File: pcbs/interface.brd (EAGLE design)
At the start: 36.3 x 29.1 mm, 26 parts, among them U1 ISL3179EIBZ, U2 ATMEGA328P

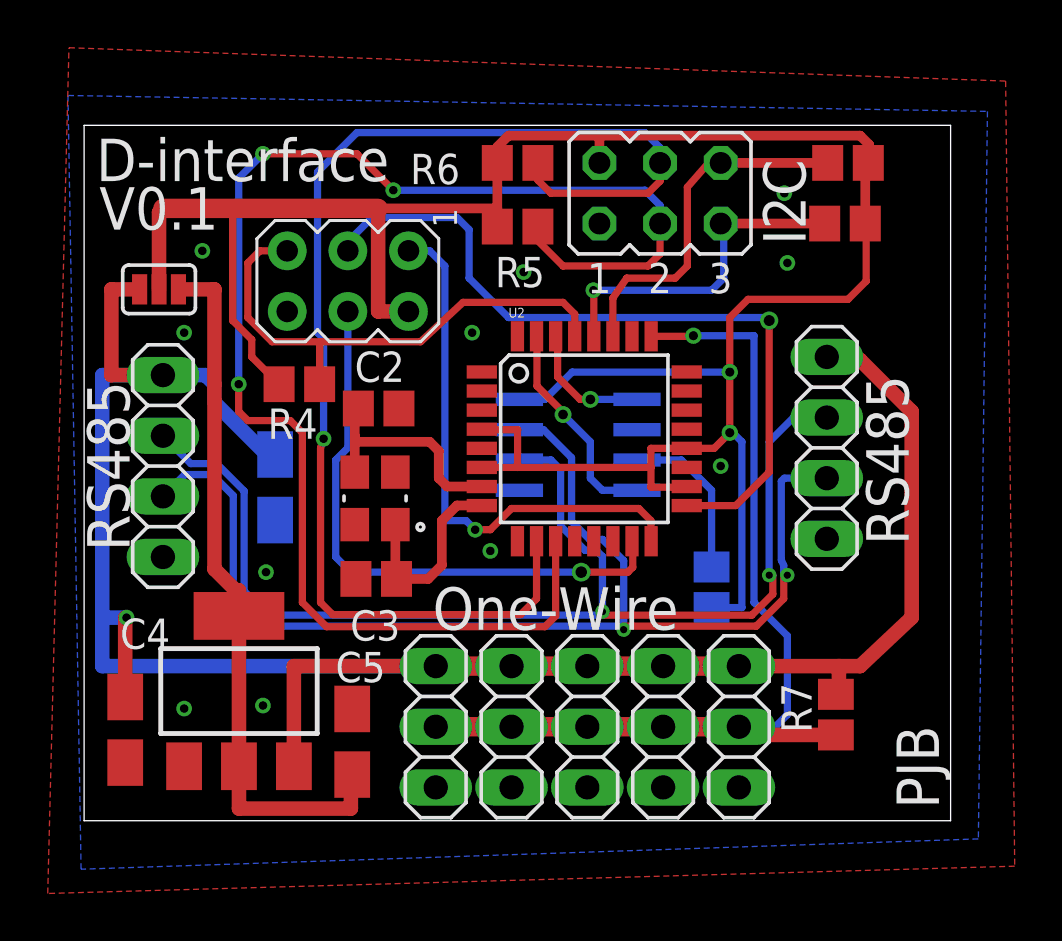
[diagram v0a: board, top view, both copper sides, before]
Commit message: Now has pin for rs485 tx enable
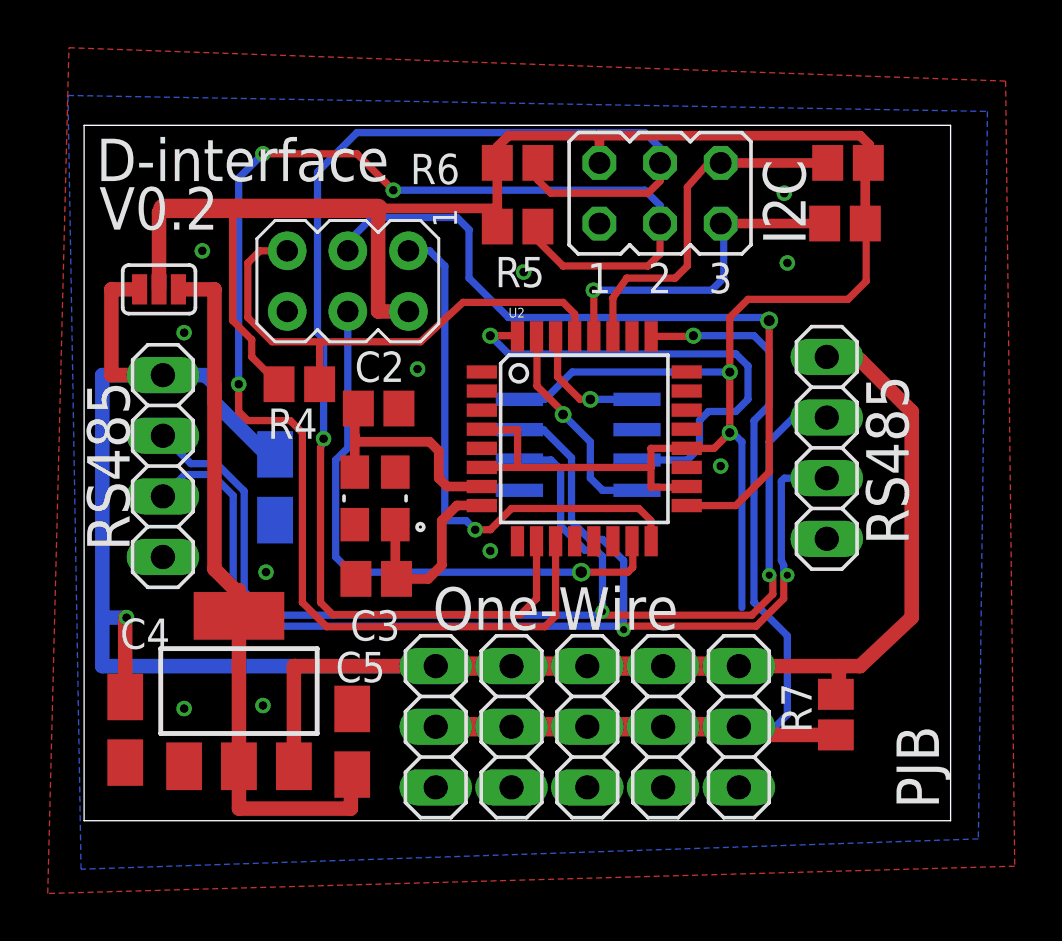
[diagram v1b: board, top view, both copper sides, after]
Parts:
- removed R1: 1k, resistor:R0805
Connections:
- removed net N$1: R1.1, U1.3
- new net TXEN: U1.3, U2.32
- net VCC: no longer R1.2
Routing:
- net TXEN: track 0.00 -> 20.2 mm, vias 0 -> 1
- net N$1: track 6.86 -> 0.00 mm
- net VCC: track 103.9 -> 102.6 mm
- net 1W: track 40.1 -> 40.7 mm
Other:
- board text added: "V0.2"
- board text removed: "V0.1"
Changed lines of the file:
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@@
 <?xml version="1.0" encoding="utf-8"?>
 <!DOCTYPE eagle SYSTEM "eagle.dtd">
-<eagle version="6.5.0">
+<eagle version="6.6.0">
 <drawing>
 <settings>
@@
 <grid distance="5" unitdist="mil" unit="mil" style="lines" multiple="1" display="yes" altdistance="1" altunitdist="mil" altunit="mil"/>
 <layers>
-<layer number="1" name="Top" color="4" fill="1" visible="no" active="yes"/>
+<layer number="1" name="Top" color="4" fill="1" visible="yes" active="yes"/>
 <layer number="2" name="Route2" color="1" fill="3" visible="no" active="no"/>
 <layer number="3" name="Route3" color="4" fill="3" visible="no" active="no"/>
@@
 <layer number="14" name="Route14" color="1" fill="6" visible="no" active="no"/>
 <layer number="15" name="Route15" color="4" fill="6" visible="no" active="no"/>
-<layer number="16" name="Bottom" color="1" fill="1" visible="no" active="yes"/>
-<layer number="17" name="Pads" color="2" fill="1" visible="no" active="yes"/>
-<layer number="18" name="Vias" color="2" fill="1" visible="no" active="yes"/>
-<layer number="19" name="Unrouted" color="6" fill="1" visible="no" active="yes"/>
+<layer number="16" name="Bottom" color="1" fill="1" visible="yes" active="yes"/>
+<layer number="17" name="Pads" color="2" fill="1" visible="yes" active="yes"/>
+<layer number="18" name="Vias" color="2" fill="1" visible="yes" active="yes"/>
+<layer number="19" name="Unrouted" color="6" fill="1" visible="yes" active="yes"/>
 <layer number="20" name="Dimension" color="15" fill="1" visible="yes" active="yes"/>
-<layer number="21" name="tPlace" color="7" fill="1" visible="no" active="yes"/>
-<layer number="22" name="bPlace" color="7" fill="1" visible="no" active="yes"/>
-<layer number="23" name="tOrigins" color="15" fill="1" visible="no" active="yes"/>
-<layer number="24" name="bOrigins" color="15" fill="1" visible="no" active="yes"/>
-<layer number="25" name="tNames" color="7" fill="1" visible="no" active="yes"/>
-<layer number="26" name="bNames" color="7" fill="1" visible="no" active="yes"/>
-<layer number="27" name="tValues" color="7" fill="1" visible="no" active="yes"/>
-<layer number="28" name="bValues" color="7" fill="1" visible="no" active="yes"/>
+<layer number="21" name="tPlace" color="7" fill="1" visible="yes" active="yes"/>
+<layer number="22" name="bPlace" color="7" fill="1" visible="yes" active="yes"/>
+<layer number="23" name="tOrigins" color="15" fill="1" visible="yes" active="yes"/>
+<layer number="24" name="bOrigins" color="15" fill="1" visible="yes" active="yes"/>
+<layer number="25" name="tNames" color="7" fill="1" visible="yes" active="yes"/>
+<layer number="26" name="bNames" color="7" fill="1" visible="yes" active="yes"/>
+<layer number="27" name="tValues" color="7" fill="1" visible="yes" active="yes"/>
+<layer number="28" name="bValues" color="7" fill="1" visible="yes" active="yes"/>
 <layer number="29" name="tStop" color="7" fill="3" visible="no" active="yes"/>
 <layer number="30" name="bStop" color="7" fill="6" visible="no" active="yes"/>
 <layer number="31" name="tCream" color="7" fill="4" visible="no" active="yes"/>
-<layer number="32" name="bCream" color="7" fill="5" visible="yes" active="yes"/>
+<layer number="32" name="bCream" color="7" fill="5" visible="no" active="yes"/>
 <layer number="33" name="tFinish" color="6" fill="3" visible="no" active="yes"/>
 <layer number="34" name="bFinish" color="6" fill="6" visible="no" active="yes"/>
@@
 <layer number="43" name="vRestrict" color="2" fill="10" visible="no" active="yes"/>
 <layer number="44" name="Drills" color="7" fill="1" visible="no" active="yes"/>
-<layer number="45" name="Holes" color="7" fill="1" visible="no" active="yes"/>
+<layer number="45" name="Holes" color="7" fill="1" visible="yes" active="yes"/>
 <layer number="46" name="Milling" color="3" fill="1" visible="no" active="yes"/>
 <layer number="47" name="Measures" color="7" fill="1" visible="no" active="yes"/>
@@
 <wire x1="-38.989" y1="27.229" x2="-38.989" y2="-1.905" width="0" layer="20"/>
 <text x="-38.481" y="24.892" size="1.778" layer="25">D-interface</text>
-<text x="-38.354" y="22.86" size="1.778" layer="25">V0.1</text>
+<text x="-38.354" y="22.86" size="1.778" layer="25">V0.2</text>
 <text x="-3.175" y="-1.397" size="1.778" layer="25" rot="R90">PJB</text>
 <text x="-24.384" y="6.096" size="1.778" layer="25">One-Wire</text>
@@
 <attribute name="VALUE" x="-33.313" y="10.115" size="1.27" layer="28" rot="MR90"/>
 </element>
-<element name="R1" library="resistor" package="R0805" value="1k" x="-12.7" y="7.874" smashed="yes" rot="MR270"/>
 <element name="ISP1" library="adafruit" package="AVRISP" value="AVRISP-6" x="-27.94" y="20.701" smashed="yes" rot="R270"/>
 <element name="JP2" library="pinhead" package="1X04" value="" x="-7.874" y="13.716" smashed="yes" rot="R270">
@@
 <via x="-12.319" y="12.954" extent="1-16" drill="0.3556" diameter="0.508"/>
 <via x="-9.525" y="21.463" extent="1-16" drill="0.3556" diameter="0.508"/>
-<via x="-22.733" y="18.542" extent="1-16" drill="0.3556" diameter="0.508"/>
+<via x="-25.019" y="17.018" extent="1-16" drill="0.3556" diameter="0.508"/>
 <via x="-20.574" y="21.082" extent="1-16" drill="0.3556" diameter="0.508"/>
 </signal>
@@
 <contactref element="ISP1" pad="2"/>
 <contactref element="U1" pad="8"/>
-<contactref element="R1" pad="2"/>
 <contactref element="U2" pad="18"/>
 <contactref element="U2" pad="4"/>
@@
 <wire x1="-35.85" y1="20.357" x2="-35.85" y2="23.586" width="0.6096" layer="1"/>
 <wire x1="-35.85" y1="23.586" x2="-35.687" y2="23.749" width="0.6096" layer="1"/>
-<wire x1="-12.7" y1="7.024" x2="-11.43" y2="7.024" width="0.3048" layer="16"/>
 <wire x1="-11.43" y1="7.024" x2="-11.43" y2="13.97" width="0.3048" layer="16"/>
 <via x="-11.938" y="14.351" extent="1-16" drill="0.381"/>
@@
 <wire x1="-20.0152" y1="18.3708" x2="-20.034" y2="18.3896" width="0.3048" layer="1"/>
 </signal>
-<signal name="N$1">
+<signal name="TXEN">
 <contactref element="U1" pad="3"/>
-<contactref element="R1" pad="1"/>
-<wire x1="-12.7" y1="8.724" x2="-12.7" y2="11.938" width="0.3048" layer="16"/>
-<wire x1="-12.7" y1="11.938" x2="-13.97" y2="13.208" width="0.3048" layer="16"/>
-<wire x1="-13.97" y1="13.208" x2="-15.8242" y2="13.208" width="0.3048" layer="16"/>
+<contactref element="U2" pad="32"/>
+<wire x1="-15.8242" y1="13.208" x2="-13.716" y2="13.208" width="0.3048" layer="16"/>
+<wire x1="-13.716" y1="13.208" x2="-13.208" y2="13.716" width="0.3048" layer="16"/>
+<wire x1="-13.208" y1="13.716" x2="-13.208" y2="14.859" width="0.3048" layer="16"/>
+<wire x1="-13.208" y1="14.859" x2="-12.827" y2="15.24" width="0.3048" layer="16"/>
+<wire x1="-12.827" y1="15.24" x2="-11.684" y2="15.24" width="0.3048" layer="16"/>
+<wire x1="-11.684" y1="15.24" x2="-11.176" y2="15.748" width="0.3048" layer="16"/>
+<wire x1="-11.176" y1="15.748" x2="-11.176" y2="17.145" width="0.3048" layer="16"/>
+<wire x1="-11.176" y1="17.145" x2="-11.684" y2="17.653" width="0.3048" layer="16"/>
+<wire x1="-11.684" y1="17.653" x2="-21.209" y2="17.653" width="0.3048" layer="16"/>
+<wire x1="-21.209" y1="17.653" x2="-21.971" y2="18.415" width="0.3048" layer="16"/>
+<via x="-21.971" y="18.415" extent="1-16" drill="0.381"/>
+<wire x1="-21.971" y1="18.415" x2="-20.8594" y2="18.415" width="0.3048" layer="1"/>
+<wire x1="-20.8594" y1="18.415" x2="-20.834" y2="18.3896" width="0.3048" layer="1"/>
 </signal>
 <signal name="!RESET">
@@
 <wire x1="-13.4874" y1="18.3896" x2="-13.462" y2="18.415" width="0.3048" layer="1"/>
 <via x="-13.462" y="18.415" extent="1-16" drill="0.381"/>
-<wire x1="-13.462" y1="18.415" x2="-10.922" y2="18.415" width="0.3048" layer="16"/>
-<wire x1="-10.922" y1="18.415" x2="-10.922" y2="7.239" width="0.3048" layer="16"/>
 <wire x1="-10.922" y1="7.239" x2="-9.525" y2="5.842" width="0.3048" layer="16"/>
 <wire x1="-9.525" y1="5.842" x2="-9.525" y2="2.54" width="0.3048" layer="16"/>
@@
 <wire x1="-11.557" y1="1.69" x2="-11.557" y2="2.032" width="0.8128" layer="1"/>
 <wire x1="-7.493" y1="1.69" x2="-11.557" y2="1.69" width="0.6096" layer="1"/>
+<wire x1="-10.922" y1="7.239" x2="-10.922" y2="14.859" width="0.3048" layer="16"/>
+<wire x1="-10.922" y1="14.859" x2="-10.287" y2="15.494" width="0.3048" layer="16"/>
+<wire x1="-10.287" y1="15.494" x2="-10.287" y2="17.78" width="0.3048" layer="16"/>
+<wire x1="-10.287" y1="17.78" x2="-10.922" y2="18.415" width="0.3048" layer="16"/>
+<wire x1="-10.922" y1="18.415" x2="-13.462" y2="18.415" width="0.3048" layer="16"/>
 </signal>
 <signal name="N$2">

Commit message: now has control of rx as well
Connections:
- net GND: no longer U1.2
- net TXEN: now also U1.2
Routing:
- net TXEN: track 20.2 -> 21.5 mm
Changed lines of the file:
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@@
 <signal name="GND">
 <contactref element="U1" pad="5"/>
-<contactref element="U1" pad="2"/>
 <contactref element="ISP1" pad="6"/>
 <contactref element="JP1" pad="4"/>
@@
 <wire x1="-21.971" y1="18.415" x2="-20.8594" y2="18.415" width="0.3048" layer="1"/>
 <wire x1="-20.8594" y1="18.415" x2="-20.834" y2="18.3896" width="0.3048" layer="1"/>
+<contactref element="U1" pad="2"/>
+<wire x1="-15.8242" y1="14.478" x2="-15.8242" y2="13.208" width="0.4064" layer="16"/>
 </signal>
 <signal name="!RESET">
